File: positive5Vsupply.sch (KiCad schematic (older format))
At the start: 18 parts, among them U3 LT3959

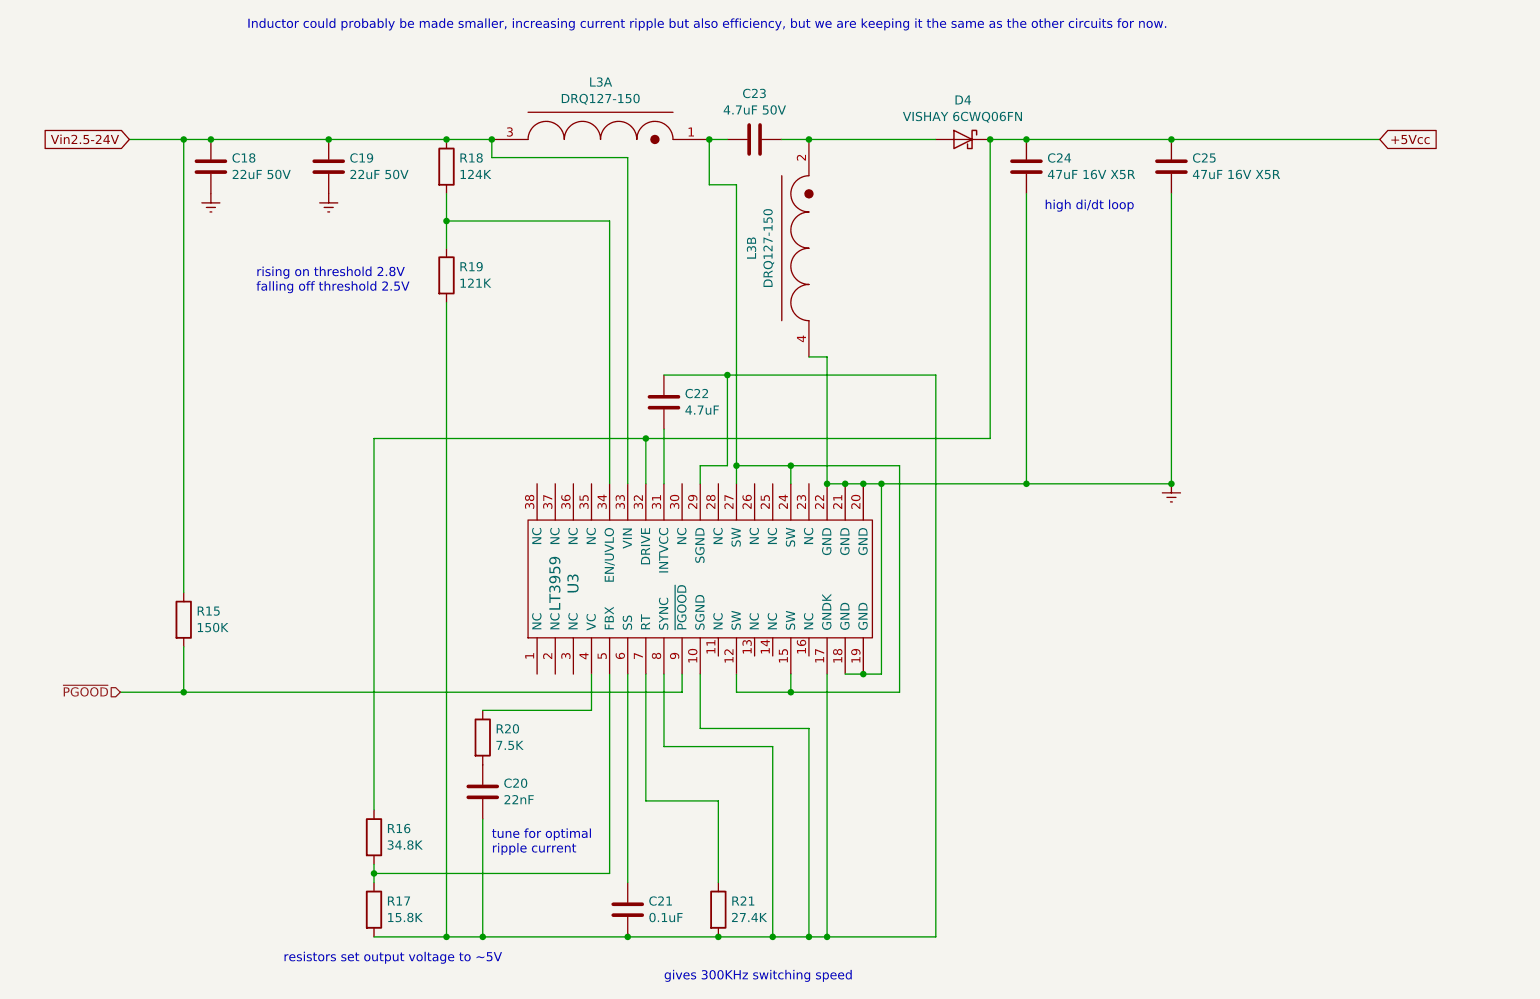
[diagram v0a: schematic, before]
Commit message: Named nets, made it use 2 inductors
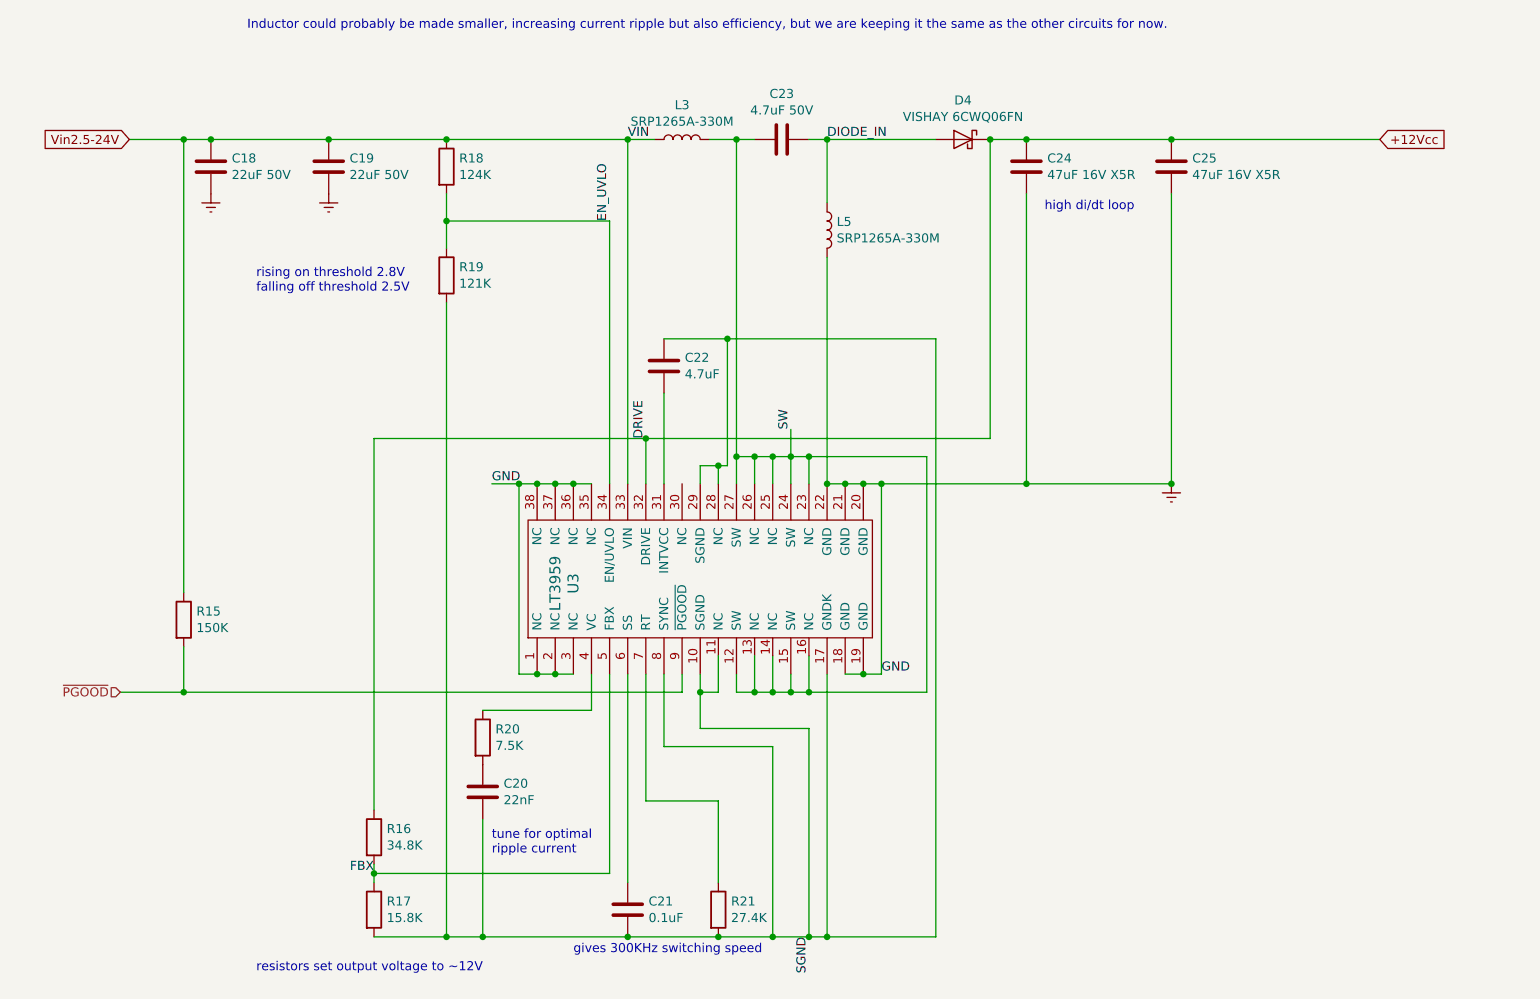
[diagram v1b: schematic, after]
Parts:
- removed L3: DRQ127-150, eaton:eaton_drq127, symbol coiltronics:DRQ127-150
- added L3, L5: SRP1265A-330M, bourns:bourns_srp1265a, symbol Device:L
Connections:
- net Earth: now also U3.1 (NC), U3.2 (NC), U3.3 (NC), U3.35 (NC), U3.36 (NC), U3.37 (NC), U3.38 (NC), L5.2
- net Vin2.5-24V: now also L3.1
- net EN_UVLO: now reaches R18.2, R19.1, U3.34 (EN/UVLO)
- net SGND: now reaches C20.2, C21.2, C22.1, R17.2, R19.2, R21.2, U3.10 (SGND), U3.17 (GNDK), U3.29 (SGND), U3.8 (SYNC)
- net SGND: now also U3.11 (NC), U3.28 (NC)
- net SW: now reaches C23.1, U3.12 (SW), U3.15 (SW), U3.24 (SW), U3.27 (SW)
- net SW: now also U3.13 (NC), U3.14 (NC), U3.16 (NC), U3.23 (NC), U3.25 (NC), U3.26 (NC), L3.2
- net DIODE_IN: now reaches C23.2, D4.2 (A)
- net DIODE_IN: now also L5.1
- net FBX: now reaches R16.2, R17.1, U3.5 (FBX)
- net +5Vcc renamed +12Vcc
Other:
- note added: "resistors set output voltage to ~~12V"
- note removed: "resistors set output voltage to ~~5V"

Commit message: Use better footprint for TO-252 diode package
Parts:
- D4: footprint Package_TO_SOT_SMD:TO-252-2 -> generic:D_TO-252
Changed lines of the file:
@@
 F 0 "D4" H 6250 1566 50  0000 C CNN
 F 1 "VISHAY 6CWQ06FN" H 6250 1475 50  0000 C CNN
-F 2 "Package_TO_SOT_SMD:TO-252-2" H 6250 1350 50  0001 C CNN
+F 2 "generic:D_TO-252" H 6250 1350 50  0001 C CNN
 F 3 "~" H 6250 1350 50  0001 C CNN
 	1    6250 1350
